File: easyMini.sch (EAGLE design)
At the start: 41 parts

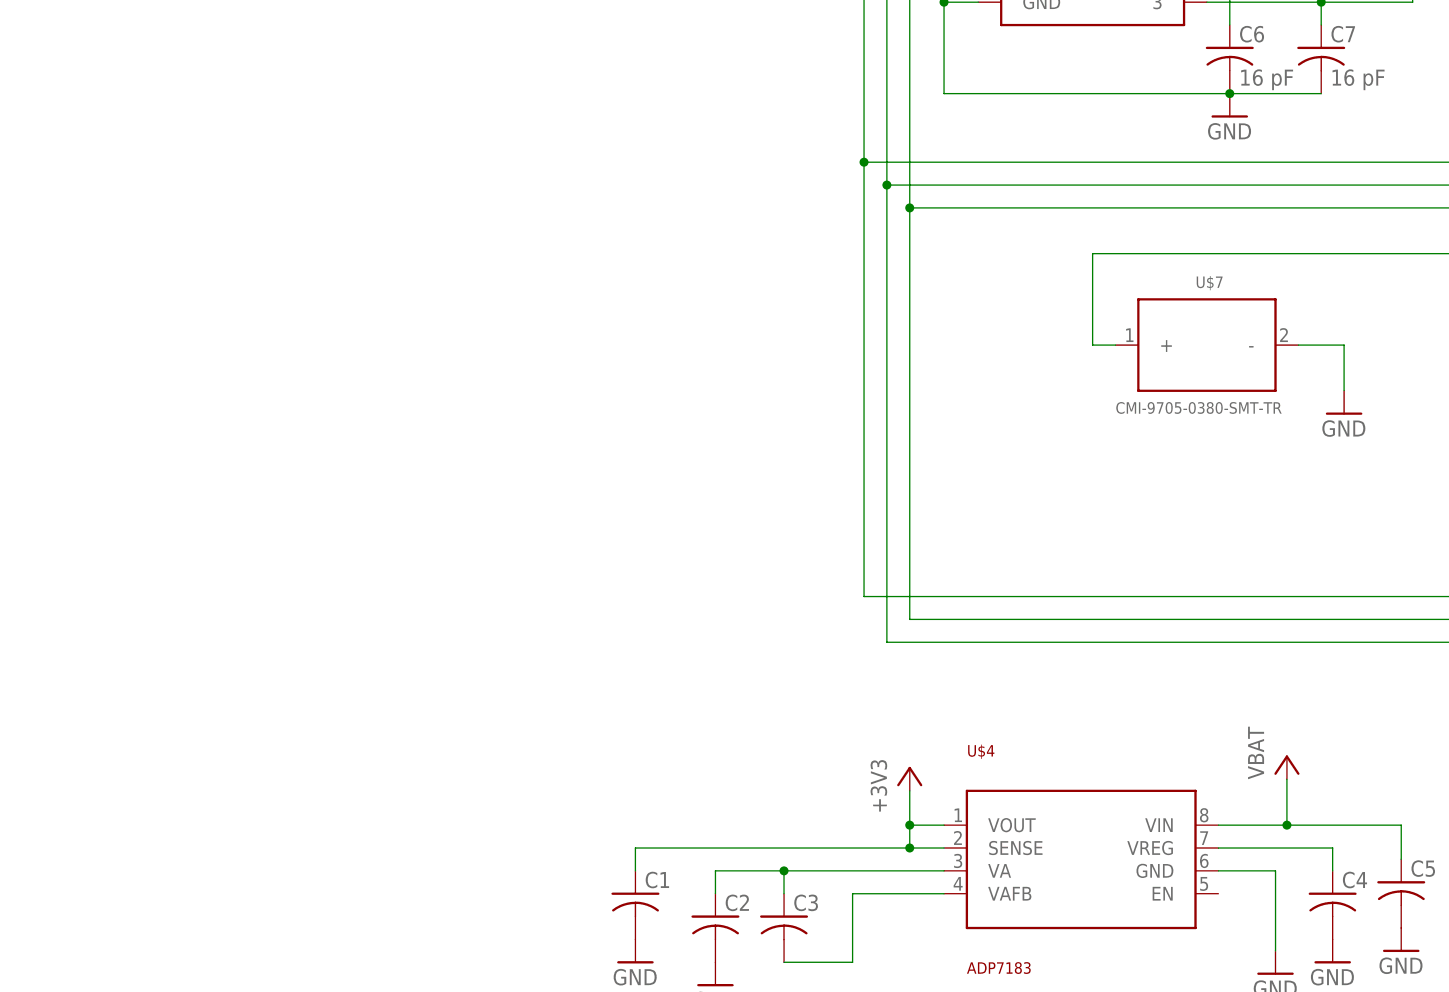
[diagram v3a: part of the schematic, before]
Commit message: Added reverse polarity protection and battery/switch connectors. Continued board design organization:
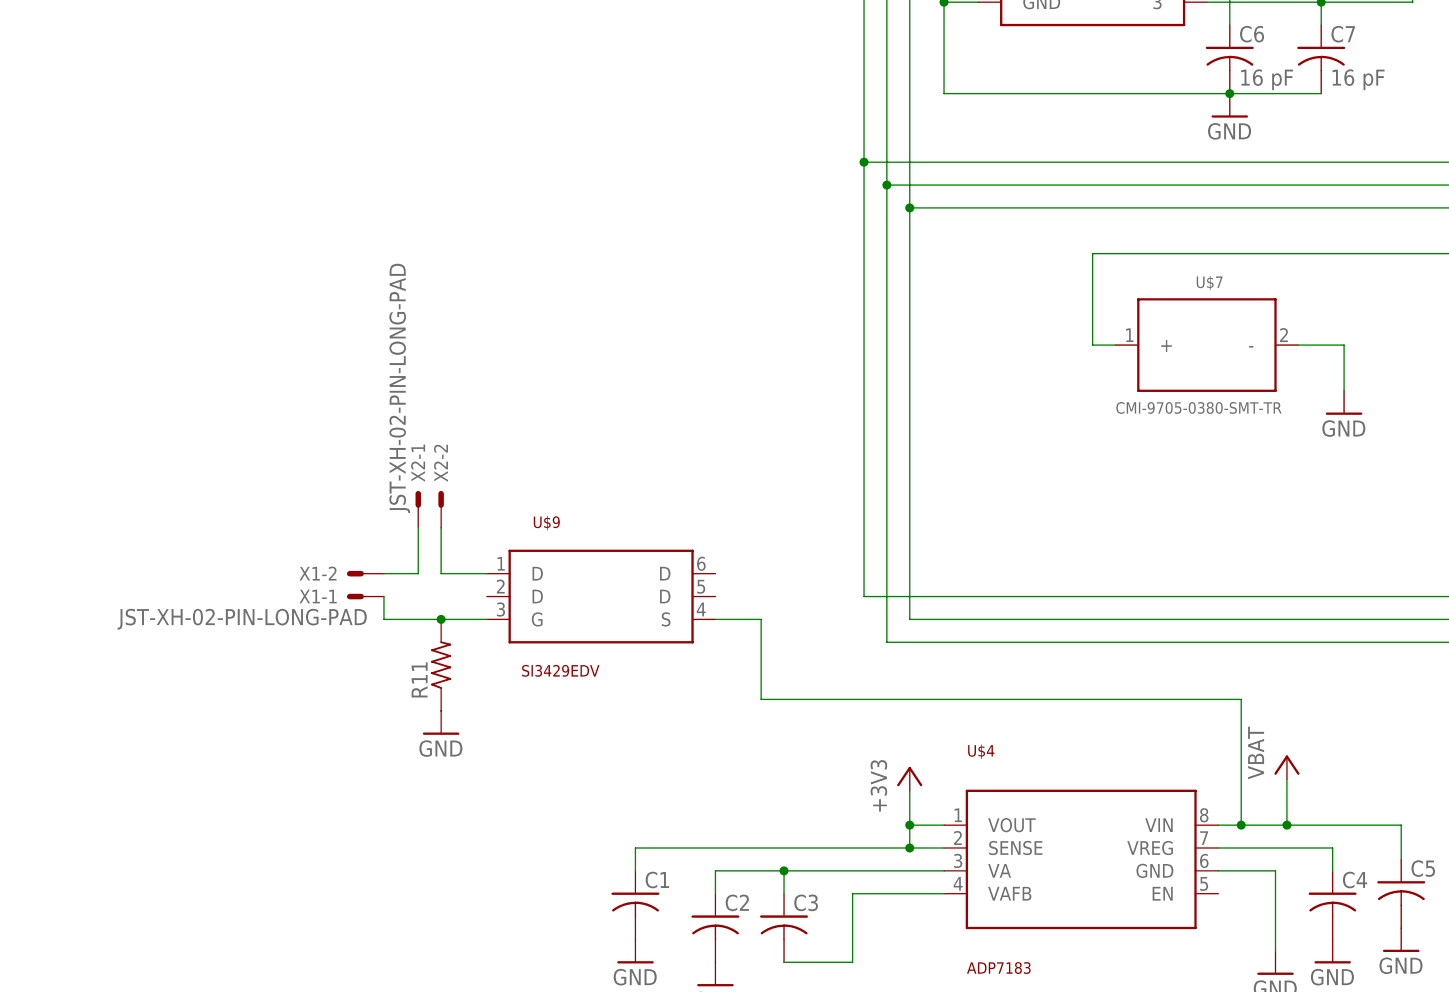
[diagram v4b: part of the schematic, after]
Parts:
- added R11: (no value), rcl:R-US_M0805
- added U$9: SI3429EDV, generalUse:SI3429EDV
- added X1, X2: JST-XH-02-PIN-LONG-PAD, Rembrandt Electronics - JST XH Connectors v1-0:JST-XH-02-PIN-LONG-PAD
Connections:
- new net N$23: X1-2.S, X2-1.S
- new net N$26: R11.2, U$9.G, X1-1.S
- new net N$27: U$9.D@1, X2-2.S
- net GND: now also R11.1
- net VCC: now also U$9.S
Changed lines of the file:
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@@
 <part name="GND23" library="supply1" library_urn="urn:adsk.eagle:library:371" deviceset="GND" device=""/>
 <part name="+3V8" library="supply1" library_urn="urn:adsk.eagle:library:371" deviceset="+3V3" device="" value="VBAT"/>
+<part name="X1" library="Rembrandt Electronics - JST XH Connectors v1-0" deviceset="JST-XH-02-PIN" device="-LONG-PAD"/>
+<part name="U$9" library="generalUse" deviceset="SI3429EDV" device=""/>
+<part name="R11" library="rcl" library_urn="urn:adsk.eagle:library:334" deviceset="R-US_" device="M0805" package3d_urn="urn:adsk.eagle:package:23556/2"/>
+<part name="GND24" library="supply1" library_urn="urn:adsk.eagle:library:371" deviceset="GND" device=""/>
+<part name="X2" library="Rembrandt Electronics - JST XH Connectors v1-0" deviceset="JST-XH-02-PIN" device="-LONG-PAD"/>
 </parts>
 <sheets>
@@
 <instance part="+3V8" gate="G$1" x="205.74" y="-12.7" smashed="yes">
 <attribute name="VALUE" x="203.2" y="-17.78" size="1.778" layer="96" rot="R90"/>
+</instance>
+<instance part="X1" gate="-2" x="-147.32" y="-50.8" smashed="yes" rot="R180">
+<attribute name="NAME" x="-149.86" y="-50.038" size="1.524" layer="95" rot="R180"/>
+</instance>
+<instance part="X1" gate="-1" x="-147.32" y="-53.34" smashed="yes" rot="R180">
+<attribute name="NAME" x="-149.86" y="-52.578" size="1.524" layer="95" rot="R180"/>
+<attribute name="VALUE" x="-146.558" y="-54.737" size="1.778" layer="96" rot="R180"/>
+</instance>
+<instance part="U$9" gate="G$1" x="-120.65" y="-53.34" smashed="yes">
+<attribute name="NAME" x="-128.27" y="-45.72" size="1.27" layer="94"/>
+<attribute name="VALUE" x="-129.54" y="-62.23" size="1.27" layer="94"/>
+</instance>
+<instance part="R11" gate="G$1" x="-138.43" y="-60.96" smashed="yes" rot="R90">
+<attribute name="NAME" x="-139.9286" y="-64.77" size="1.778" layer="95" rot="R90"/>
+<attribute name="VALUE" x="-135.128" y="-64.77" size="1.778" layer="96" rot="R90"/>
+</instance>
+<instance part="GND24" gate="1" x="-138.43" y="-68.58" smashed="yes">
+<attribute name="VALUE" x="-140.97" y="-71.12" size="1.778" layer="96"/>
+</instance>
+<instance part="X2" gate="-2" x="-138.43" y="-43.18" smashed="yes" rot="R90">
+<attribute name="NAME" x="-137.668" y="-40.64" size="1.524" layer="95" rot="R90"/>
+</instance>
+<instance part="X2" gate="-1" x="-140.97" y="-43.18" smashed="yes" rot="R90">
+<attribute name="NAME" x="-140.208" y="-40.64" size="1.524" layer="95" rot="R90"/>
+<attribute name="VALUE" x="-142.367" y="-43.942" size="1.778" layer="96" rot="R90"/>
 </instance>
 </instances>
@@
 <pinref part="C13" gate="G$1" pin="2"/>
 </segment>
+<segment>
+<pinref part="R11" gate="G$1" pin="1"/>
+<pinref part="GND24" gate="1" pin="GND"/>
+</segment>
 </net>
 <net name="+3V3" class="0">
@@
 <segment>
 <pinref part="U$4" gate="G$1" pin="VIN"/>
-<wire x1="-52.07" y1="-78.74" x2="-44.45" y2="-78.74" width="0.1524" layer="91"/>
+<wire x1="-52.07" y1="-78.74" x2="-49.53" y2="-78.74" width="0.1524" layer="91"/>
 <pinref part="P+1" gate="VCC" pin="VCC"/>
+<wire x1="-49.53" y1="-78.74" x2="-44.45" y2="-78.74" width="0.1524" layer="91"/>
 <wire x1="-44.45" y1="-73.66" x2="-44.45" y2="-78.74" width="0.1524" layer="91"/>
 <wire x1="-31.75" y1="-78.74" x2="-44.45" y2="-78.74" width="0.1524" layer="91"/>
@@
 <wire x1="-31.75" y1="-78.74" x2="-31.75" y2="-82.55" width="0.1524" layer="91"/>
 <pinref part="C5" gate="G$1" pin="1"/>
+<pinref part="U$9" gate="G$1" pin="S"/>
+<wire x1="-107.95" y1="-55.88" x2="-102.87" y2="-55.88" width="0.1524" layer="91"/>
+<wire x1="-102.87" y1="-55.88" x2="-102.87" y2="-64.77" width="0.1524" layer="91"/>
+<wire x1="-102.87" y1="-64.77" x2="-49.53" y2="-64.77" width="0.1524" layer="91"/>
+<wire x1="-49.53" y1="-64.77" x2="-49.53" y2="-78.74" width="0.1524" layer="91"/>
+<junction x="-49.53" y="-78.74"/>
 </segment>
 </net>
@@
 </segment>
 </net>
+<net name="N$26" class="0">
+<segment>
+<pinref part="X1" gate="-1" pin="S"/>
+<pinref part="U$9" gate="G$1" pin="G"/>
+<wire x1="-144.78" y1="-53.34" x2="-144.78" y2="-55.88" width="0.1524" layer="91"/>
+<wire x1="-144.78" y1="-55.88" x2="-138.43" y2="-55.88" width="0.1524" layer="91"/>
+<pinref part="R11" gate="G$1" pin="2"/>
+<wire x1="-138.43" y1="-55.88" x2="-133.35" y2="-55.88" width="0.1524" layer="91"/>
+<junction x="-138.43" y="-55.88"/>
+</segment>
+</net>
+<net name="N$23" class="0">
+<segment>
+<pinref part="X1" gate="-2" pin="S"/>
+<pinref part="X2" gate="-1" pin="S"/>
+<wire x1="-144.78" y1="-50.8" x2="-140.97" y2="-50.8" width="0.1524" layer="91"/>
+<wire x1="-140.97" y1="-50.8" x2="-140.97" y2="-45.72" width="0.1524" layer="91"/>
+</segment>
+</net>
+<net name="N$27" class="0">
+<segment>
+<pinref part="X2" gate="-2" pin="S"/>
+<wire x1="-138.43" y1="-45.72" x2="-138.43" y2="-50.8" width="0.1524" layer="91"/>
+<pinref part="U$9" gate="G$1" pin="D@1"/>
+<wire x1="-138.43" y1="-50.8" x2="-133.35" y2="-50.8" width="0.1524" layer="91"/>
+</segment>
+</net>

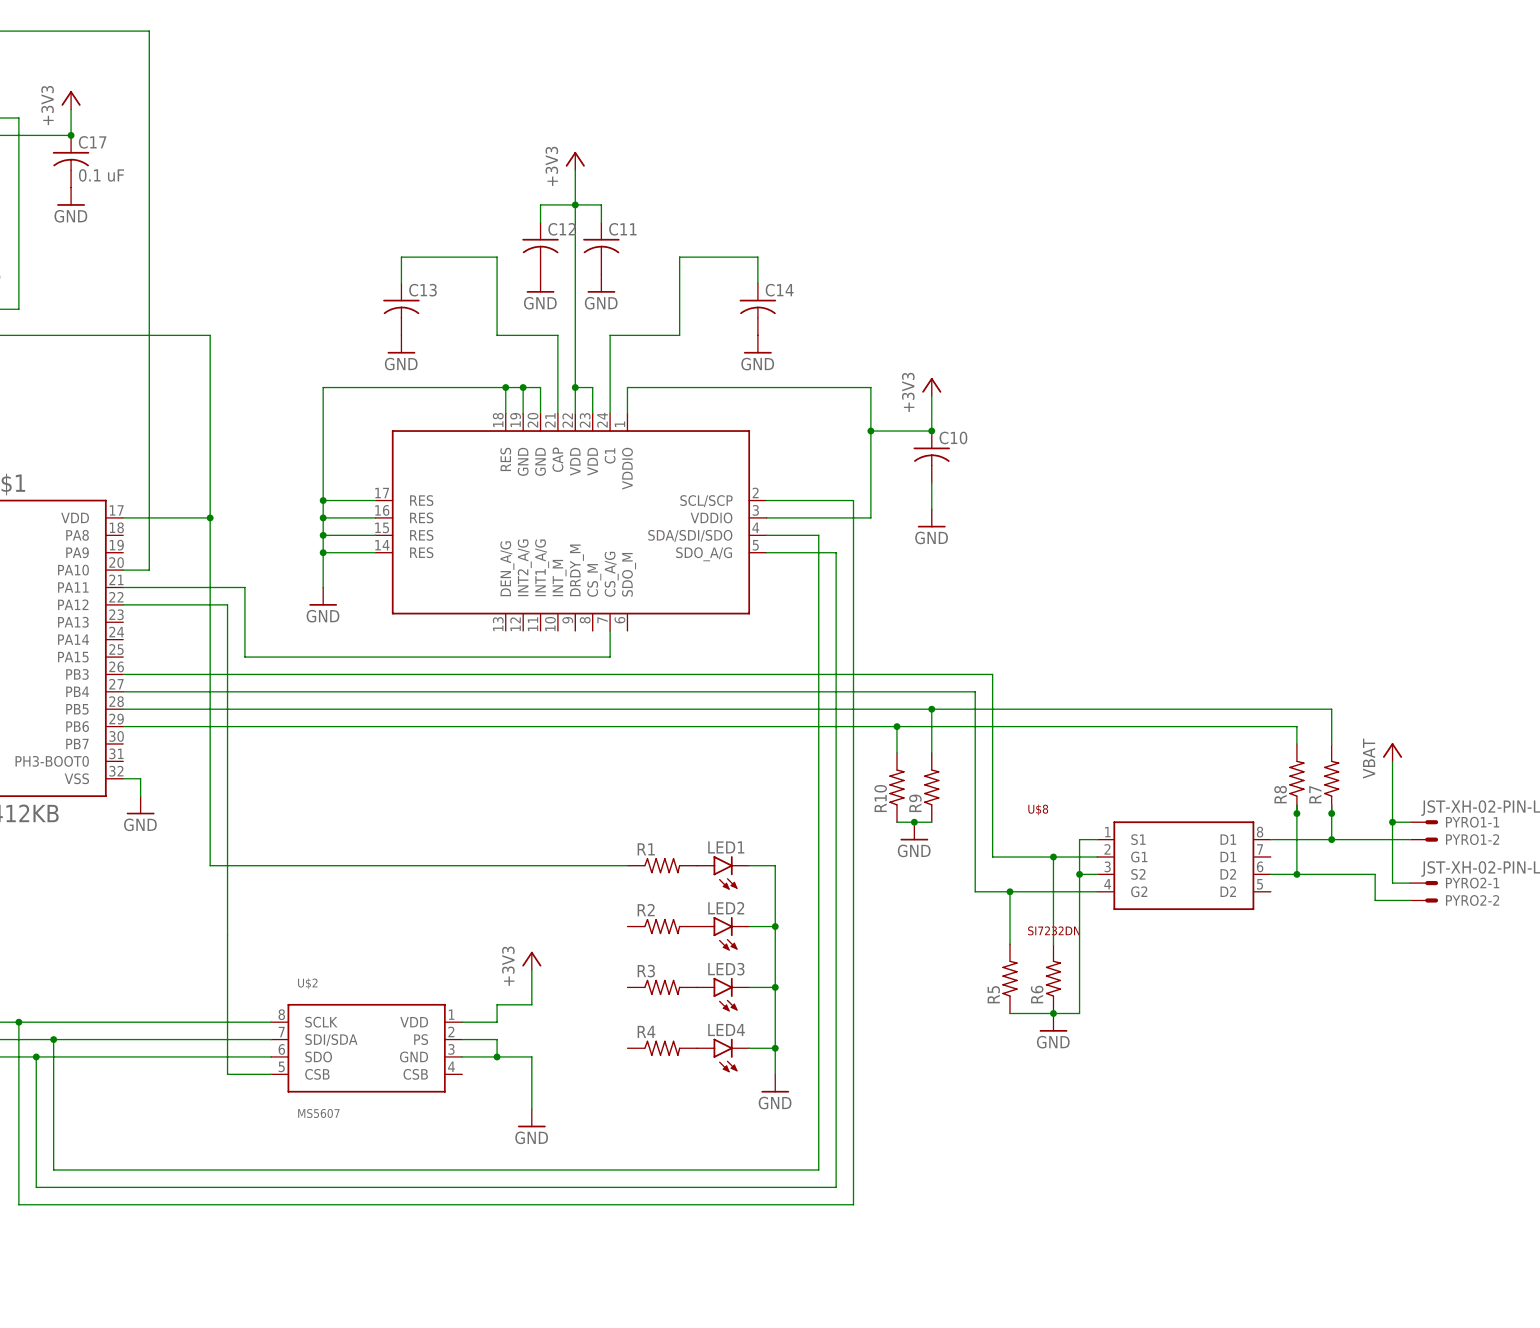
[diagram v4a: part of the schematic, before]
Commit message: Shrink board and organization of two layers into more sensible layout. Changed pins to allow USB addition on microcontroller.
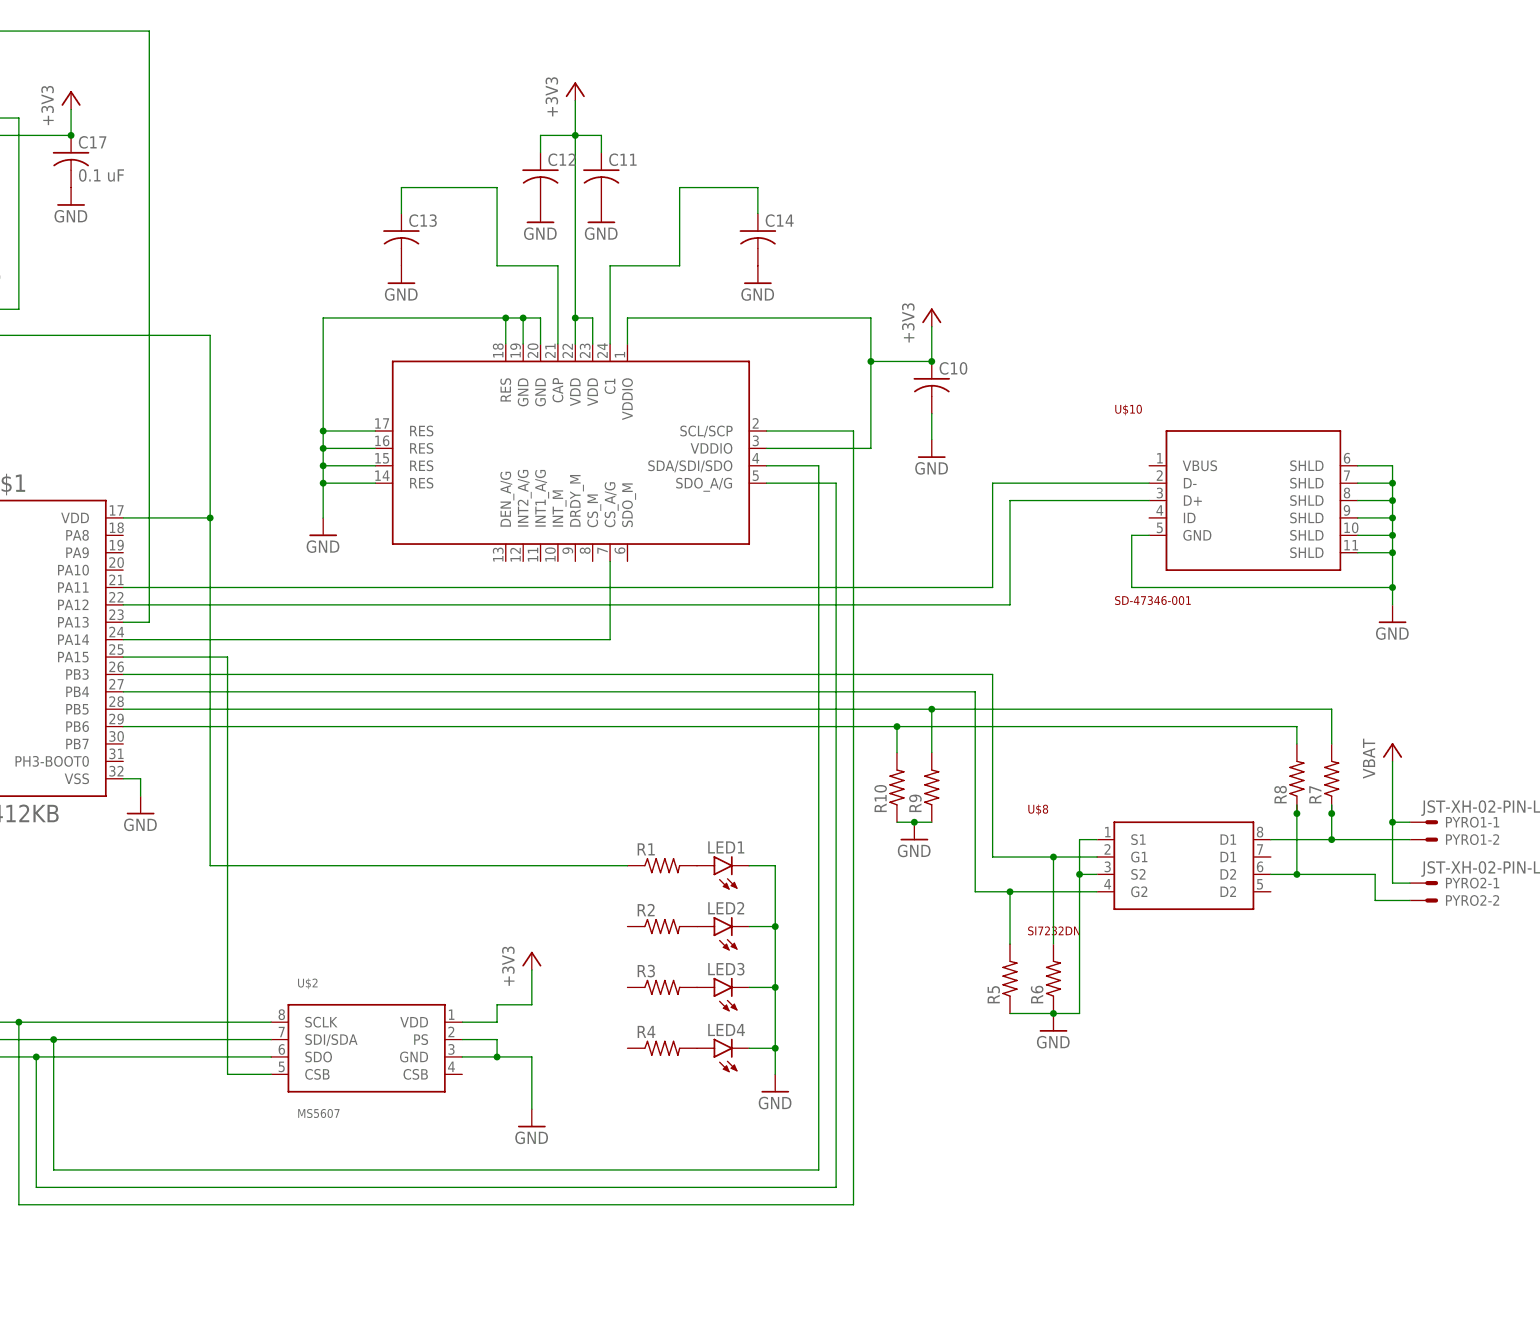
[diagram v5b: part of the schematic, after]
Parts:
- added U$10: SD-47346-001, generalUse:SD-47346-001
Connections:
- new net N$28: U$1.PA11, U$10.D-
- new net N$29: U$1.PA12, U$10.D+
- net GND: now also U$10.GND, U$10.SHLD@10, U$10.SHLD@11, U$10.SHLD@6, U$10.SHLD@7, U$10.SHLD@8, U$10.SHLD@9
- net N$15: now also U$1.PA14; no longer U$1.PA11
- net N$16: now also U$1.PA15; no longer U$1.PA12
- net N$9: now also U$1.PA13; no longer U$1.PA10
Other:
- moved on the sheet: C10, C11, C12, C13, C14
